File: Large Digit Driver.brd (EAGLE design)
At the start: 45.7 x 30.5 mm, 25 parts, among them U1 TPIC6B595PTH

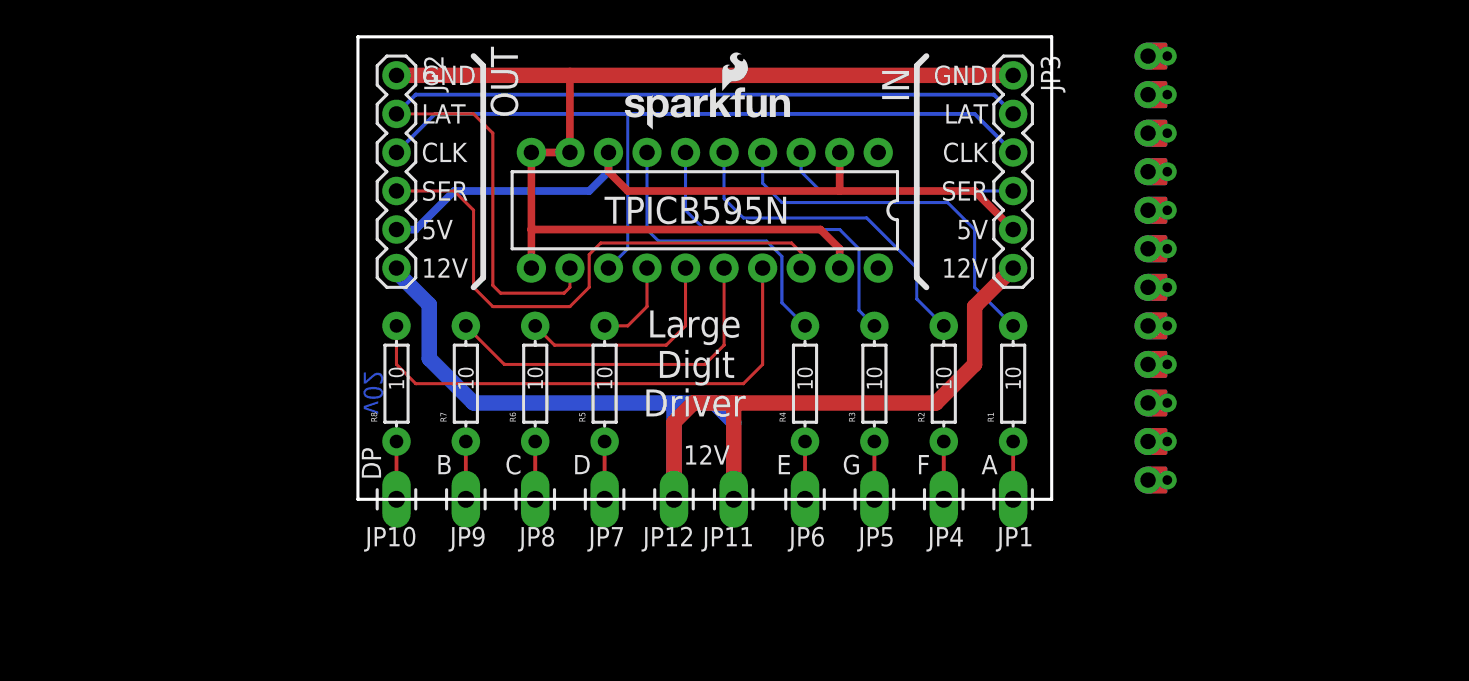
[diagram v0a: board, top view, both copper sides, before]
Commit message: Conversion to SMD parts.
Board is much smaller. Uses TPIC6C596.
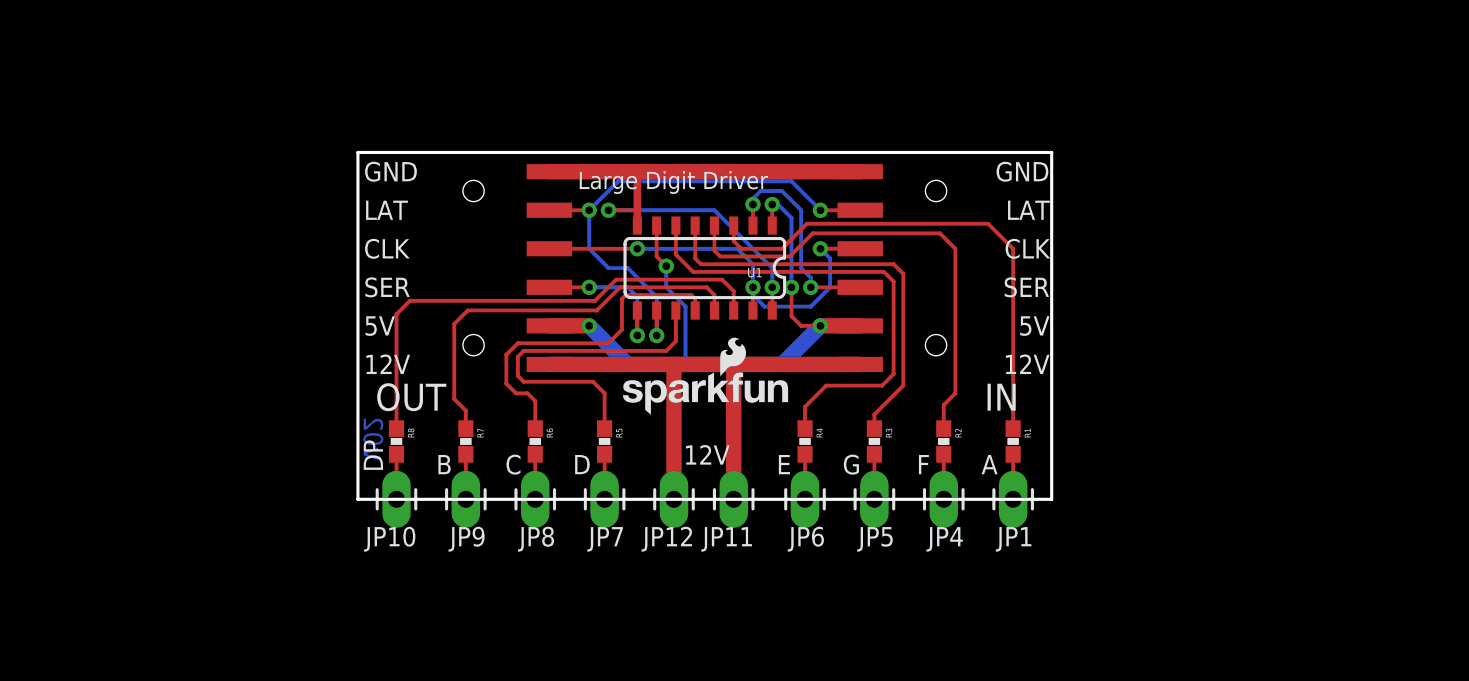
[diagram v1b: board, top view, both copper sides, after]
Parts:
- removed JP3: IN, SparkFun-Connectors:1X06
- JP13: value M12PTH-CST-L -> IN; device Spark:1X12-CASTELLATED -> SparkFun-Connectors:1X06-SMD
- JP2: device SparkFun-Connectors:1X06 -> SparkFun-Connectors:1X06-SMD
- R1, R2, R3, R4, R5, R6, R7, R8: value 10 -> 20; device SparkFun-Resistors:AXIAL-0.3 -> SparkFun-Resistors:0603-RES
- U1: value TPIC6B595PTH -> TPIC6C596; device SparkFun-DigitalIC:DIL20 -> SparkFun-DigitalIC:SO016
- moved LOGO2 25.4 mm to (43.2, 3.81)
- moved LOGO1 18.8 mm to (17.0, 5.46)
- moved JP13 14.0 mm to (38.1, 15.2), turned to 90 degrees
- moved JP2 13.7 mm to (7.62, 15.2)
- moved U1 3.81 mm to (22.9, 15.2)
- moved R1 3.81 mm to (43.2, 3.81), turned to 270 degrees
- moved R2 3.81 mm to (38.6, 3.81), turned to 270 degrees
- moved R3 3.81 mm to (34.0, 3.81), turned to 270 degrees
- moved R4 3.81 mm to (29.5, 3.81), turned to 270 degrees
- moved R5 3.81 mm to (16.3, 3.81), turned to 270 degrees
- moved R6 3.81 mm to (11.7, 3.81), turned to 270 degrees
- moved R7 3.81 mm to (7.11, 3.81), turned to 270 degrees
- moved R8 3.81 mm to (2.54, 3.81), turned to 270 degrees
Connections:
- net 12V: now also JP13.1; no longer JP3.6
- net 5V: now also JP13.2, U1.1, U1.7; no longer JP3.5, U1.2, U1.8
- net CLOCK: now also JP13.4, U1.15; no longer JP3.3, U1.13
- net D0: now also R1.1, U1.3; no longer R1.P$2, U1.4
- net D1: now also R2.1, U1.4; no longer R2.P$2, U1.5
- net D2: now also R3.1, U1.5; no longer R3.P$2, U1.6
- net D3: now also R4.1, U1.6; no longer R4.P$2, U1.7
- net D4: now also R5.1, U1.11; no longer R5.P$2, U1.14
- net D5: now also R6.1, U1.12; no longer R6.P$2, U1.15
- net D6: now also R7.1, U1.13; no longer R7.P$2, U1.16
- net D7: now also R8.1, U1.14; no longer R8.P$2, U1.17
- net GND: now also JP13.6, U1.16, U1.8; no longer JP3.1, U1.10, U1.11, U1.19, U1.9
- net LATCH: now also JP13.5, U1.10; no longer JP3.2, U1.12
- net S0: now also R1.2; no longer R1.P$1
- net S1: now also R2.2; no longer R2.P$1
- net S2: now also R3.2; no longer R3.P$1
- net S3: now also R4.2; no longer R4.P$1
- net S4: now also R5.2; no longer R5.P$1
- net S5: now also R6.2; no longer R6.P$1
- net S6: now also R7.2; no longer R7.P$1
- net S7: now also R8.2; no longer R8.P$1
- net SER_IN: now also JP13.3, U1.2; no longer JP3.4, U1.3
- net SER_OUT: now also U1.9; no longer U1.18
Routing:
- net 12V: track 80.3 -> 38.3 mm
- net GND: track 78.0 -> 41.2 mm, vias 0 -> 2
- net LATCH: track 65.3 -> 34.5 mm, vias 0 -> 3
- net SER_OUT: track 37.1 -> 10.2 mm, vias 0 -> 2
- net CLOCK: track 53.4 -> 28.7 mm, vias 0 -> 3
- net D4: track 5.86 -> 22.6 mm
- net D3: track 19.9 -> 31.3 mm
- net D1: track 22.2 -> 30.9 mm
- net D0: track 24.7 -> 32.9 mm
- net D5: track 14.8 -> 22.2 mm
- net D2: track 21.8 -> 27.3 mm
- net 5V: track 48.9 -> 44.2 mm, vias 0 -> 5
- net D6: track 23.7 -> 26.6 mm
- net D7: track 34.1 -> 32.3 mm
- net SER_IN: track 15.8 -> 14.3 mm, vias 0 -> 2
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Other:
- board size 45.7 x 30.5 mm -> 45.7 x 22.9 mm
- board text added: "Large Digit Driver"
- board text added: "TPICC596"
- board text removed: "Digit"
- board text removed: "Driver"
- board text removed: "Large"
- board text removed: "TPICB595N"

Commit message: Removed extraneous layers.
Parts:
- moved FRAME1 28.4 mm to (-6.35, -17.8)
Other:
- board text added: "Leave room on panel for these castelated holes to be milled."
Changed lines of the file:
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@@
 <?xml version="1.0" encoding="utf-8"?>
 <!DOCTYPE eagle SYSTEM "eagle.dtd">
-<eagle version="7.1.0">
+<eagle version="7.2.0">
 <drawing>
 <settings>
@@
 <layer number="31" name="tCream" color="7" fill="4" visible="no" active="yes"/>
 <layer number="32" name="bCream" color="7" fill="5" visible="no" active="yes"/>
-<layer number="33" name="tFinish" color="6" fill="3" visible="no" active="yes"/>
-<layer number="34" name="bFinish" color="6" fill="6" visible="no" active="yes"/>
 <layer number="35" name="tGlue" color="7" fill="4" visible="no" active="yes"/>
 <layer number="36" name="bGlue" color="7" fill="5" visible="no" active="yes"/>
-<layer number="37" name="tTest" color="7" fill="1" visible="no" active="yes"/>
-<layer number="38" name="bTest" color="7" fill="1" visible="no" active="yes"/>
 <layer number="39" name="tKeepout" color="4" fill="11" visible="no" active="yes"/>
 <layer number="40" name="bKeepout" color="1" fill="11" visible="no" active="yes"/>
@@
 <layer number="45" name="Holes" color="7" fill="1" visible="yes" active="yes"/>
 <layer number="46" name="Milling" color="3" fill="1" visible="no" active="yes"/>
-<layer number="47" name="Measures" color="7" fill="1" visible="yes" active="yes"/>
+<layer number="47" name="Measures" color="7" fill="1" visible="no" active="yes"/>
 <layer number="48" name="Document" color="7" fill="1" visible="no" active="yes"/>
 <layer number="49" name="Reference" color="11" fill="1" visible="yes" active="yes"/>
-<layer number="50" name="dxf" color="7" fill="1" visible="no" active="yes"/>
 <layer number="51" name="tDocu" color="6" fill="1" visible="yes" active="yes"/>
 <layer number="52" name="bDocu" color="7" fill="1" visible="no" active="yes"/>
@@
 <layer number="99" name="SpiceOrder" color="7" fill="1" visible="no" active="no"/>
 <layer number="100" name="Muster" color="7" fill="1" visible="no" active="no"/>
-<layer number="101" name="Patch_Top" color="12" fill="4" visible="no" active="yes"/>
-<layer number="102" name="Vscore" color="7" fill="1" visible="no" active="yes"/>
-<layer number="103" name="tMap" color="7" fill="1" visible="no" active="yes"/>
-<layer number="104" name="Name" color="16" fill="1" visible="no" active="yes"/>
-<layer number="105" name="tPlate" color="7" fill="1" visible="no" active="yes"/>
-<layer number="106" name="bPlate" color="7" fill="1" visible="no" active="yes"/>
-<layer number="107" name="Crop" color="7" fill="1" visible="no" active="yes"/>
-<layer number="108" name="tplace-old" color="10" fill="1" visible="no" active="yes"/>
-<layer number="109" name="ref-old" color="11" fill="1" visible="no" active="yes"/>
-<layer number="110" name="fp0" color="7" fill="1" visible="no" active="yes"/>
-<layer number="111" name="LPC17xx" color="7" fill="1" visible="no" active="yes"/>
-<layer number="112" name="tSilk" color="7" fill="1" visible="no" active="yes"/>
-<layer number="113" name="IDFDebug" color="4" fill="1" visible="no" active="yes"/>
-<layer number="116" name="Patch_BOT" color="9" fill="4" visible="no" active="yes"/>
-<layer number="121" name="_tsilk" color="7" fill="1" visible="no" active="yes"/>
-<layer number="122" name="_bsilk" color="7" fill="1" visible="no" active="yes"/>
-<layer number="123" name="tTestmark" color="7" fill="1" visible="no" active="yes"/>
-<layer number="124" name="bTestmark" color="7" fill="1" visible="no" active="yes"/>
-<layer number="125" name="_tNames" color="7" fill="1" visible="no" active="yes"/>
-<layer number="126" name="_bNames" color="7" fill="1" visible="no" active="yes"/>
-<layer number="127" name="_tValues" color="7" fill="1" visible="no" active="yes"/>
-<layer number="128" name="_bValues" color="7" fill="1" visible="no" active="yes"/>
-<layer number="129" name="Mask" color="7" fill="1" visible="no" active="yes"/>
-<layer number="131" name="tAdjust" color="7" fill="1" visible="no" active="yes"/>
-<layer number="132" name="bAdjust" color="7" fill="1" visible="no" active="yes"/>
-<layer number="144" name="Drill_legend" color="7" fill="1" visible="no" active="yes"/>
-<layer number="150" name="Notes" color="7" fill="1" visible="no" active="yes"/>
-<layer number="151" name="HeatSink" color="7" fill="1" visible="no" active="yes"/>
-<layer number="152" name="_bDocu" color="7" fill="1" visible="no" active="yes"/>
-<layer number="153" name="FabDoc1" color="7" fill="1" visible="no" active="yes"/>
-<layer number="154" name="FabDoc2" color="7" fill="1" visible="no" active="yes"/>
-<layer number="155" name="FabDoc3" color="7" fill="1" visible="no" active="yes"/>
-<layer number="199" name="Contour" color="7" fill="1" visible="no" active="yes"/>
 <layer number="200" name="200bmp" color="1" fill="10" visible="no" active="no"/>
 <layer number="201" name="201bmp" color="2" fill="1" visible="no" active="no"/>
 <layer number="202" name="202bmp" color="3" fill="1" visible="no" active="no"/>
-<layer number="203" name="203bmp" color="4" fill="10" visible="no" active="yes"/>
-<layer number="204" name="204bmp" color="5" fill="10" visible="no" active="yes"/>
-<layer number="205" name="205bmp" color="6" fill="10" visible="no" active="yes"/>
-<layer number="206" name="206bmp" color="7" fill="10" visible="no" active="yes"/>
-<layer number="207" name="207bmp" color="8" fill="10" visible="no" active="yes"/>
-<layer number="208" name="208bmp" color="9" fill="10" visible="no" active="yes"/>
-<layer number="209" name="209bmp" color="7" fill="1" visible="no" active="yes"/>
-<layer number="210" name="210bmp" color="7" fill="1" visible="no" active="yes"/>
-<layer number="211" name="211bmp" color="7" fill="1" visible="no" active="yes"/>
-<layer number="212" name="212bmp" color="7" fill="1" visible="no" active="yes"/>
-<layer number="213" name="213bmp" color="7" fill="1" visible="no" active="yes"/>
-<layer number="214" name="214bmp" color="7" fill="1" visible="no" active="yes"/>
-<layer number="215" name="215bmp" color="7" fill="1" visible="no" active="yes"/>
-<layer number="216" name="216bmp" color="7" fill="1" visible="no" active="yes"/>
 <layer number="217" name="217bmp" color="18" fill="1" visible="no" active="no"/>
 <layer number="218" name="218bmp" color="19" fill="1" visible="no" active="no"/>
@@
 <layer number="223" name="223bmp" color="24" fill="1" visible="no" active="no"/>
 <layer number="224" name="224bmp" color="25" fill="1" visible="no" active="no"/>
-<layer number="225" name="225bmp" color="7" fill="1" visible="no" active="yes"/>
-<layer number="226" name="226bmp" color="7" fill="1" visible="no" active="yes"/>
-<layer number="227" name="227bmp" color="7" fill="1" visible="no" active="yes"/>
-<layer number="228" name="228bmp" color="7" fill="1" visible="no" active="yes"/>
-<layer number="229" name="229bmp" color="7" fill="1" visible="no" active="yes"/>
-<layer number="230" name="230bmp" color="7" fill="1" visible="no" active="yes"/>
-<layer number="231" name="231bmp" color="7" fill="1" visible="no" active="yes"/>
-<layer number="248" name="Housing" color="7" fill="1" visible="no" active="yes"/>
-<layer number="249" name="Edge" color="7" fill="1" visible="no" active="yes"/>
 <layer number="250" name="Descript" color="3" fill="1" visible="no" active="no"/>
 <layer number="251" name="SMDround" color="12" fill="11" visible="no" active="no"/>
-<layer number="254" name="cooling" color="7" fill="1" visible="no" active="yes"/>
-<layer number="255" name="routoute" color="7" fill="1" visible="no" active="yes"/>
 </layers>
 <board>
@@
 <dimension x1="0" y1="22.86" x2="45.72" y2="22.86" x3="22.86" y3="29.21" textsize="1.778" textratio="15" layer="47" unit="inch"/>
 <dimension x1="0" y1="22.86" x2="6.35" y2="22.86" x3="3.175" y3="25.4" textsize="1.778" textratio="15" layer="47" unit="inch"/>
+<text x="-20.32" y="-5.08" size="1.778" layer="20" font="vector" ratio="15">Leave room on panel for these castelated holes to be milled.</text>
 </plain>
 <attributes>
@@
 <elements>
 <element name="LOGO2" library="SparkFun-Aesthetics" package="OSHW-LOGO-S" value="OSHW-LOGOS" x="43.18" y="3.81" rot="MR0"/>
-<element name="FRAME1" library="SparkFun-Aesthetics" package="CREATIVE_COMMONS" value="" x="21.59" y="-12.7" smashed="yes">
+<element name="FRAME1" library="SparkFun-Aesthetics" package="CREATIVE_COMMONS" value="" x="-6.35" y="-17.78" smashed="yes">
 <attribute name="VERSION" value="v02" x="0.381" y="2.54" size="1.27" layer="16" font="vector" ratio="15" rot="SMR90"/>
-<attribute name="DESIGNER" value="N. Seidle" x="51.26" y="-12.7" size="1.778" layer="51"/>
+<attribute name="DESIGNER" value="N. Seidle" x="24.59" y="-17.78" size="1.778" layer="51"/>
 </element>
 <element name="JP2" library="SparkFun-Connectors" package="1X06-SMD" value="OUT" x="7.62" y="15.24" rot="R270"/>

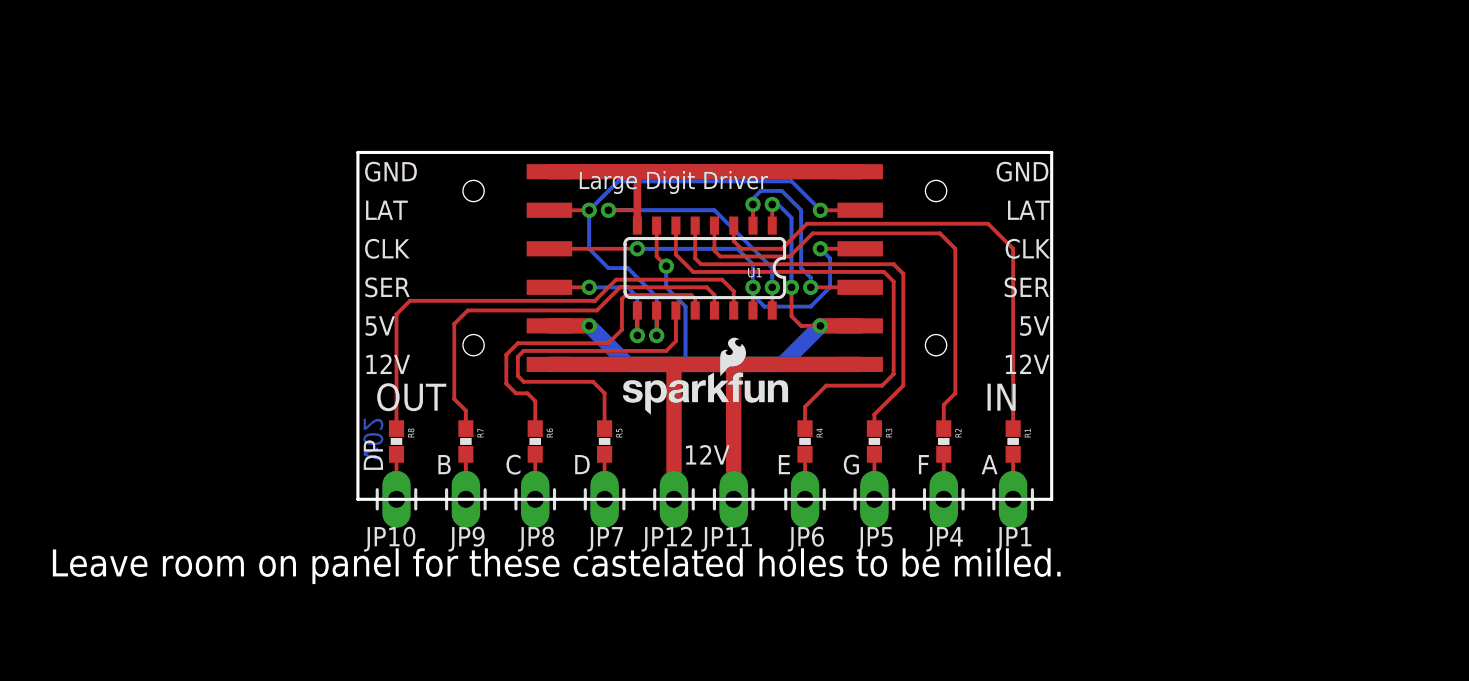
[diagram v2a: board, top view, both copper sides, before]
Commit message: Adding anchor pins for SMD mounting.
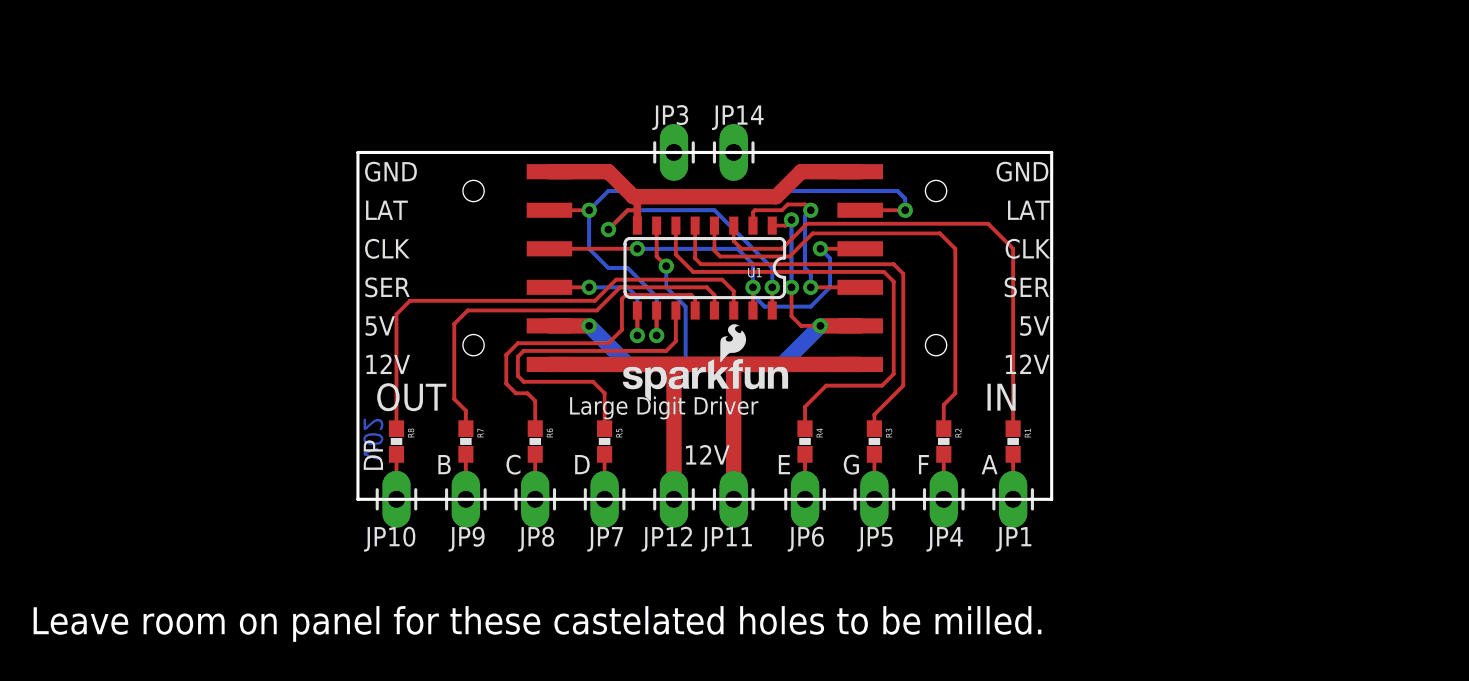
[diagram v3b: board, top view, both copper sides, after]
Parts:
- added JP14, JP3: Anchor, SparkFun-Connectors:1X01_LONGPAD
- JP13: value IN -> (none)
- JP2: value OUT -> (none)
- moved LOGO1 0.89 mm to (17.0, 6.35)
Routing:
- net LATCH: track 34.5 -> 40.4 mm
- net 5V: track 44.2 -> 42.5 mm
- net GND: track 41.2 -> 41.9 mm
- net SER_IN: track 14.3 -> 13.7 mm
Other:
- board text added: "TPIC6C596"
- board text removed: "TPICC596"
